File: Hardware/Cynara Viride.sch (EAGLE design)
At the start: 197 parts, among them Q1 TXC-7B, Q2 TXC-7WNEO, SW1 430181038816, SW2 , T1 PDTC143, T2 PDTC143, T3 PDTC143, T4 PDTC143, T5 PDTC143, U1 TM4C129EN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

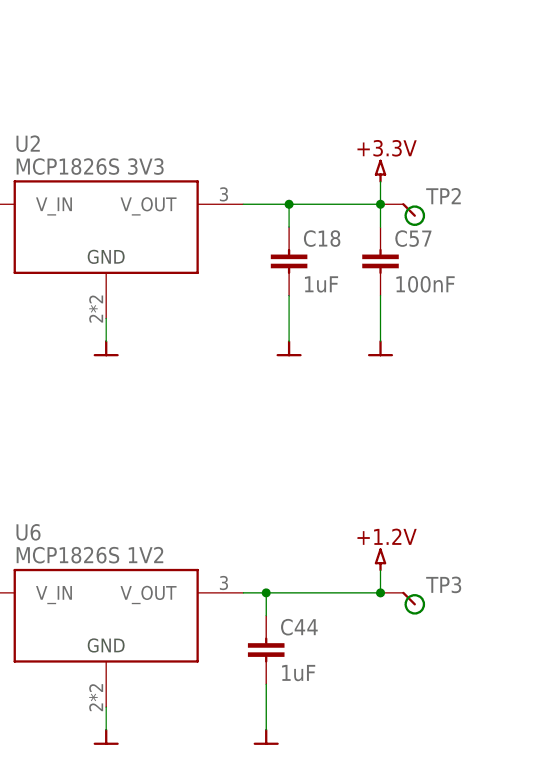
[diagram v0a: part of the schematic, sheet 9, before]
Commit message: Added jumpers to disconnect the different power rails.
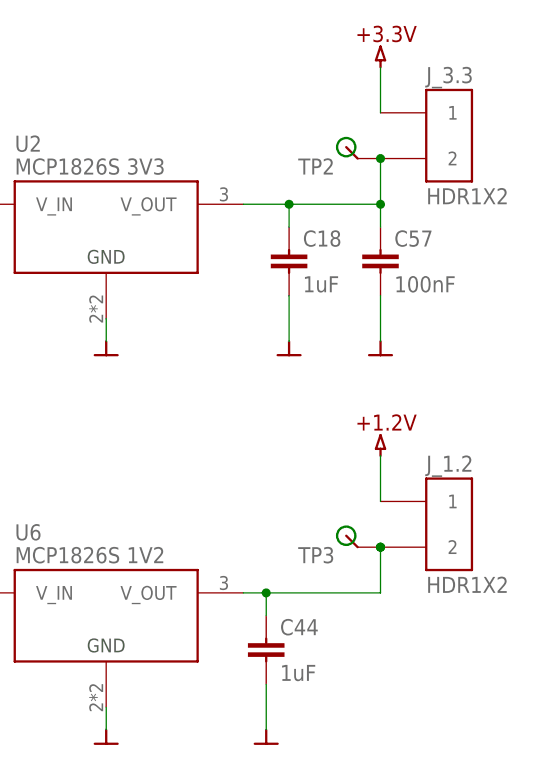
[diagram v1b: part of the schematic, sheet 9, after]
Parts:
- added J_1.2, J_3.3: HDR1X2, Cynara-Connectors:HDR1X2-M
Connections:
- new net N$10: C44.1, J_1.2.2, TP3.1, U6.V_OUT
- new net N$7: C18.1, C57.1, J_3.3.2, TP2.1, U2.V_OUT
- net +1.2V: now also J_1.2.1; no longer C44.1, TP3.1, U6.V_OUT
- net +3.3V: now also J_3.3.1; no longer C18.1, C57.1, TP2.1, U2.V_OUT
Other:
- moved on the sheet: TP2, TP3
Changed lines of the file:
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@@
 <part name="=29" library="Cynara-Symbols" deviceset="GND" device=""/>
 <part name="=30" library="Cynara-Symbols" deviceset="GND" device=""/>
-<part name="U$7" library="Cynara-Symbols" deviceset="+3.3V" device=""/>
 <part name="=31" library="Cynara-Symbols" deviceset="+5V" device=""/>
 <part name="C17" library="Cynara-Passives" deviceset="C-EU" device="C0603" value="4u7"/>
@@
 <part name="U1" library="Cynara-IntegratedCircuits" deviceset="SPLIT-TM4C129ENCPDT" device="-TQFP128" value="TM4C129EN"/>
 <part name="=169" library="Cynara-Symbols" deviceset="GND" device=""/>
+<part name="J_3.3" library="Cynara-Connectors" deviceset="HDR1X2-M" device="" value="HDR1X2"/>
+<part name="J_1.2" library="Cynara-Connectors" deviceset="HDR1X2-M" device="" value="HDR1X2"/>
+<part name="U$23" library="Cynara-Symbols" deviceset="+3.3V" device=""/>
 </parts>
 <sheets>
@@
 <instance part="U6" gate="U1" x="210.82" y="170.18"/>
 <instance part="=30" gate=" " x="210.82" y="198.12"/>
-<instance part="U$7" gate=" " x="241.3" y="220.98"/>
 <instance part="=31" gate=" " x="180.34" y="220.98"/>
 <instance part="C17" gate="G$1" x="180.34" y="210.82"/>
@@
 <instance part="=125" gate=" " x="187.96" y="154.94"/>
 <instance part="=148" gate=" " x="228.6" y="154.94"/>
-<instance part="U$22" gate="G$1" x="241.3" y="175.26"/>
+<instance part="U$22" gate="G$1" x="241.3" y="187.96"/>
 <instance part="=149" gate=" " x="210.82" y="154.94"/>
 <instance part="SW2" gate="SW1" x="78.74" y="129.54"/>
@@
 <instance part="L5" gate="G$1" x="48.26" y="81.28" rot="R90"/>
 <instance part="TP1" gate=" " x="180.34" y="215.9" rot="R180"/>
-<instance part="TP2" gate=" " x="241.3" y="215.9"/>
-<instance part="TP3" gate=" " x="241.3" y="172.72"/>
+<instance part="TP2" gate=" " x="241.3" y="220.98" rot="R180"/>
+<instance part="TP3" gate=" " x="241.3" y="177.8" rot="R180"/>
 <instance part="TP4" gate=" " x="180.34" y="203.2" rot="R180"/>
 <instance part="TP5" gate=" " x="187.96" y="160.02" rot="R180"/>
+<instance part="J_3.3" gate="X1" x="243.84" y="228.6"/>
+<instance part="J_1.2" gate="X1" x="243.84" y="185.42"/>
+<instance part="U$23" gate=" " x="241.3" y="233.68"/>
 </instances>
 <busses>
@@
 </segment>
 </net>
-<net name="+3.3V" class="0">
-<segment>
-<pinref part="U$7" gate=" " pin="+3.3V"/>
-<wire x1="241.3" y1="213.36" x2="241.3" y2="215.9" width="0.1524" layer="91"/>
-<pinref part="C57" gate="G$1" pin="1"/>
-<pinref part="U2" gate="U1" pin="V_OUT"/>
-<wire x1="241.3" y1="215.9" x2="241.3" y2="218.44" width="0.1524" layer="91"/>
-<wire x1="226.06" y1="215.9" x2="231.14" y2="215.9" width="0.1524" layer="91"/>
-<junction x="241.3" y="215.9"/>
-<pinref part="C18" gate="G$1" pin="1"/>
-<wire x1="231.14" y1="215.9" x2="241.3" y2="215.9" width="0.1524" layer="91"/>
-<wire x1="231.14" y1="213.36" x2="231.14" y2="215.9" width="0.1524" layer="91"/>
-<junction x="231.14" y="215.9"/>
-<pinref part="TP2" gate=" " pin="1"/>
-</segment>
-</net>
 <net name="+1.2V" class="0">
 <segment>
-<pinref part="U6" gate="U1" pin="V_OUT"/>
-<wire x1="226.06" y1="172.72" x2="228.6" y2="172.72" width="0.1524" layer="91"/>
 <pinref part="U$22" gate="G$1" pin="+1.2V"/>
-<wire x1="228.6" y1="172.72" x2="241.3" y2="172.72" width="0.1524" layer="91"/>
-<wire x1="241.3" y1="172.72" x2="241.3" y2="175.26" width="0.1524" layer="91"/>
-<pinref part="C44" gate="G$1" pin="1"/>
-<wire x1="228.6" y1="170.18" x2="228.6" y2="172.72" width="0.1524" layer="91"/>
-<junction x="228.6" y="172.72"/>
-<pinref part="TP3" gate=" " pin="1"/>
-<junction x="241.3" y="172.72"/>
+<wire x1="241.3" y1="182.88" x2="241.3" y2="187.96" width="0.1524" layer="91"/>
+<pinref part="J_1.2" gate="X1" pin="1"/>
 </segment>
 </net>
@@
 </segment>
 </net>
+<net name="N$7" class="0">
+<segment>
+<wire x1="241.3" y1="213.36" x2="241.3" y2="215.9" width="0.1524" layer="91"/>
+<pinref part="C57" gate="G$1" pin="1"/>
+<pinref part="U2" gate="U1" pin="V_OUT"/>
+<wire x1="241.3" y1="215.9" x2="241.3" y2="220.98" width="0.1524" layer="91"/>
+<wire x1="226.06" y1="215.9" x2="231.14" y2="215.9" width="0.1524" layer="91"/>
+<junction x="241.3" y="220.98"/>
+<pinref part="C18" gate="G$1" pin="1"/>
+<wire x1="231.14" y1="213.36" x2="231.14" y2="215.9" width="0.1524" layer="91"/>
+<junction x="231.14" y="215.9"/>
+<pinref part="TP2" gate=" " pin="1"/>
+<pinref part="J_3.3" gate="X1" pin="2"/>
+<wire x1="231.14" y1="215.9" x2="241.3" y2="215.9" width="0.1524" layer="91"/>
+<junction x="241.3" y="215.9"/>
+</segment>
+</net>
+<net name="+3.3V" class="0">
+<segment>
+<pinref part="U$23" gate=" " pin="+3.3V"/>
+<wire x1="241.3" y1="231.14" x2="241.3" y2="226.06" width="0.1524" layer="91"/>
+<pinref part="J_3.3" gate="X1" pin="1"/>
+</segment>
+</net>
+<net name="N$10" class="0">
+<segment>
+<pinref part="U6" gate="U1" pin="V_OUT"/>
+<wire x1="226.06" y1="172.72" x2="228.6" y2="172.72" width="0.1524" layer="91"/>
+<wire x1="228.6" y1="172.72" x2="241.3" y2="172.72" width="0.1524" layer="91"/>
+<wire x1="241.3" y1="172.72" x2="241.3" y2="177.8" width="0.1524" layer="91"/>
+<pinref part="C44" gate="G$1" pin="1"/>
+<wire x1="228.6" y1="170.18" x2="228.6" y2="172.72" width="0.1524" layer="91"/>
+<junction x="228.6" y="172.72"/>
+<pinref part="TP3" gate=" " pin="1"/>
+<junction x="241.3" y="177.8"/>
+<pinref part="J_1.2" gate="X1" pin="2"/>
+<junction x="241.3" y="177.8"/>
+</segment>
+</net>

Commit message: Added more test points.
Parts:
- added TP10, TP12, TP13, TP14, TP15, TP16, TP17, TP18, TP19, TP20, TP21, TP22, TP23, TP24, TP6, TP7, TP8, TP9: (no value), Cynara-Misc:TESTPAD-SMD
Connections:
- net !HIB: now also TP8.1
- net !RST: now also TP6.1
- net !WAKE: now also TP7.1
- net DONE: now also TP21.1
- net INIT: now also TP20.1
- net M0: now also TP10.1
- net M1: now also TP9.1
- net PF0_ETH: now also TP24.1
- net PF1_LEDR: now also TP16.1
- net PF2_LEDB: now also TP18.1
- net PF3_LEDG: now also TP17.1
- net PF4_ETH: now also TP23.1
- net PROGRAM: now also TP19.1
- net SSI0CLK: now also TP12.1
- net SSI0D0: now also TP13.1
- net SSI0D1: now also TP14.1
- net SSI0FSS: now also TP15.1
- net USB_DETECT: now also TP22.1
